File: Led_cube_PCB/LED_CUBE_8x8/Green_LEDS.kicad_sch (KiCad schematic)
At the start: 34 parts, among them IC1 74AHCT244PW,118, IC10 74AHCT244PW,118, IC11 74AHCT244PW,118, IC12 74AHCT244PW,118, IC2 74AHCT244PW,118, IC26 74AHC138PW,118, IC3 74AHCT244PW,118, IC8 74AHCT244PW,118, IC9 74AHCT244PW,118

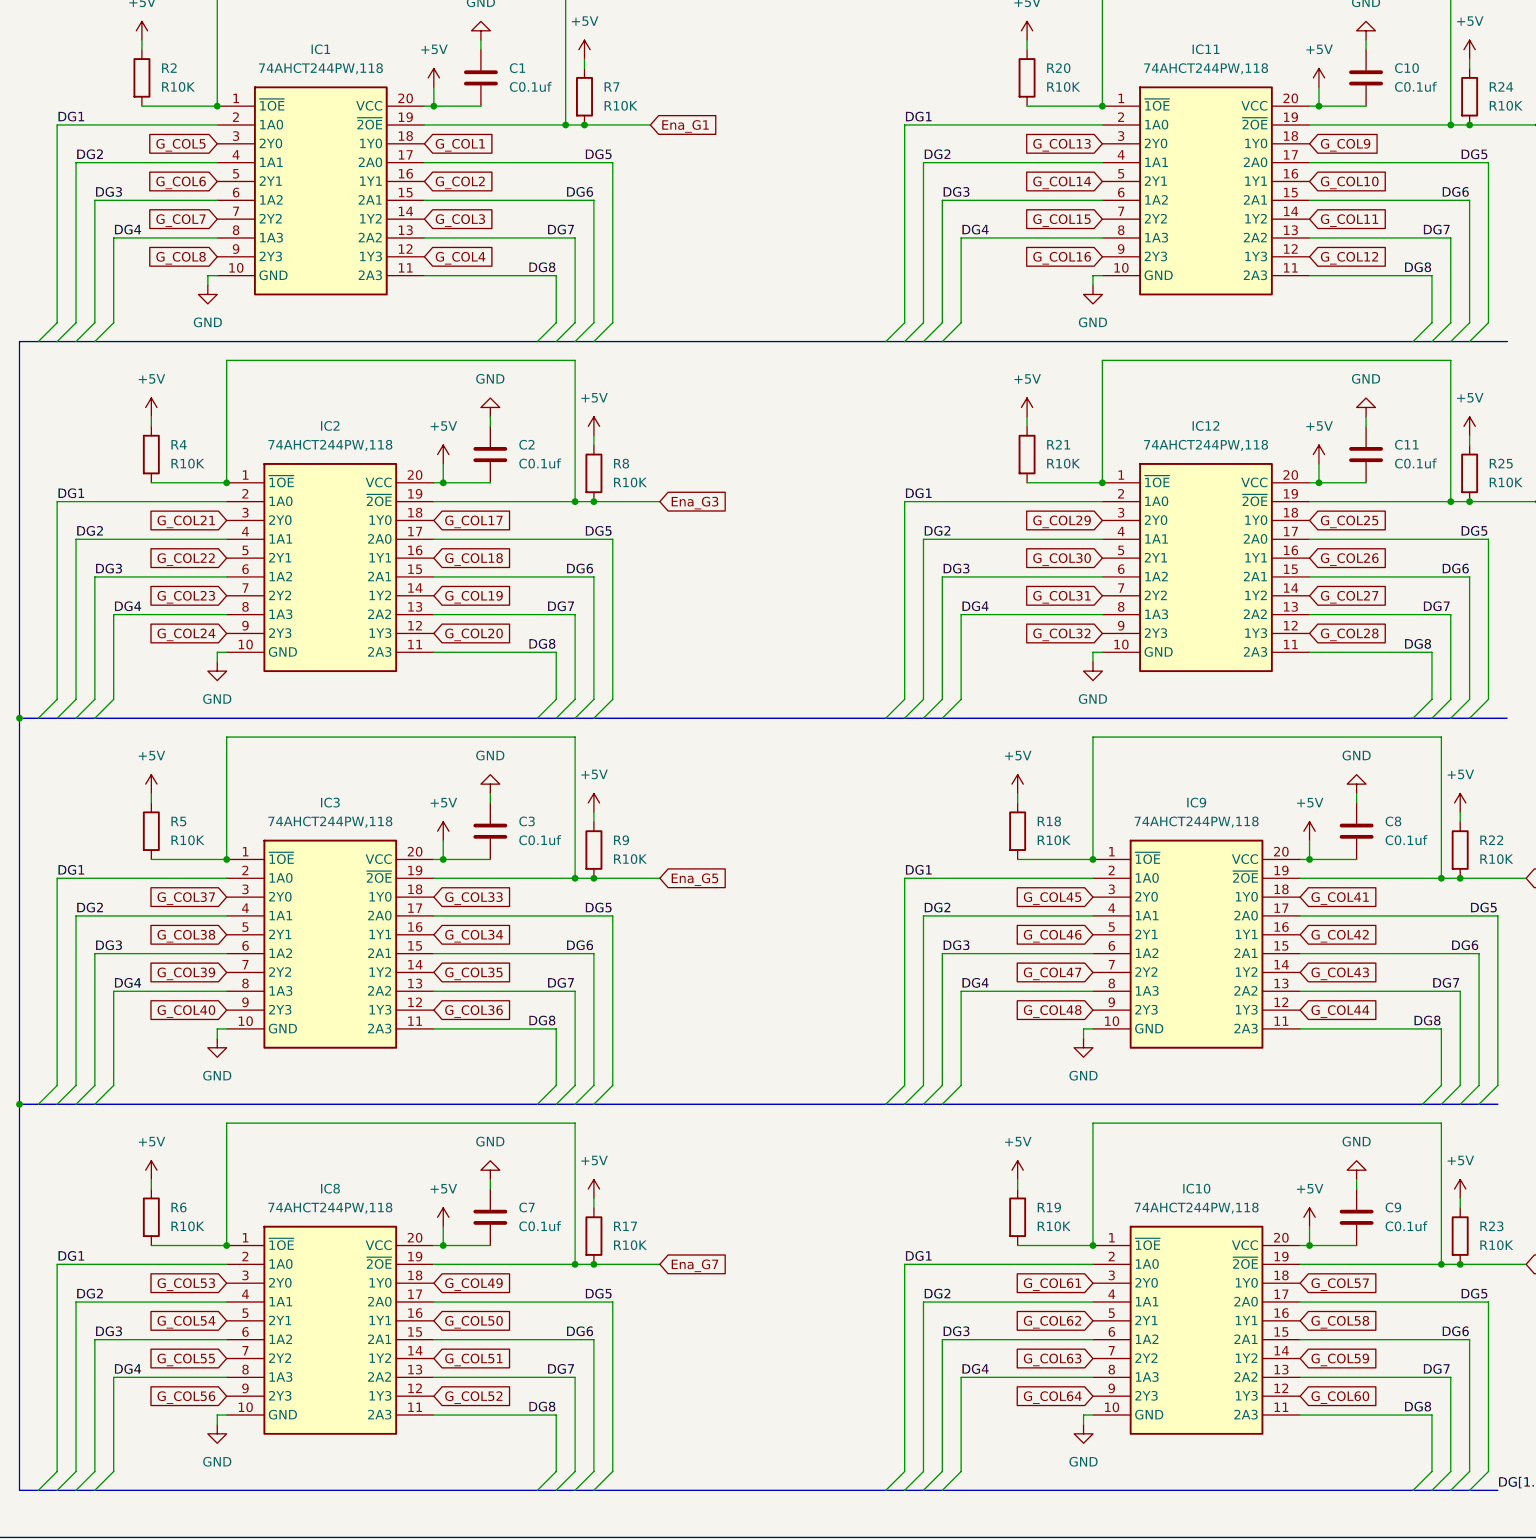
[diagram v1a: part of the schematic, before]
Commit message: added power schematic and updated labels to correct type e.g. output, input
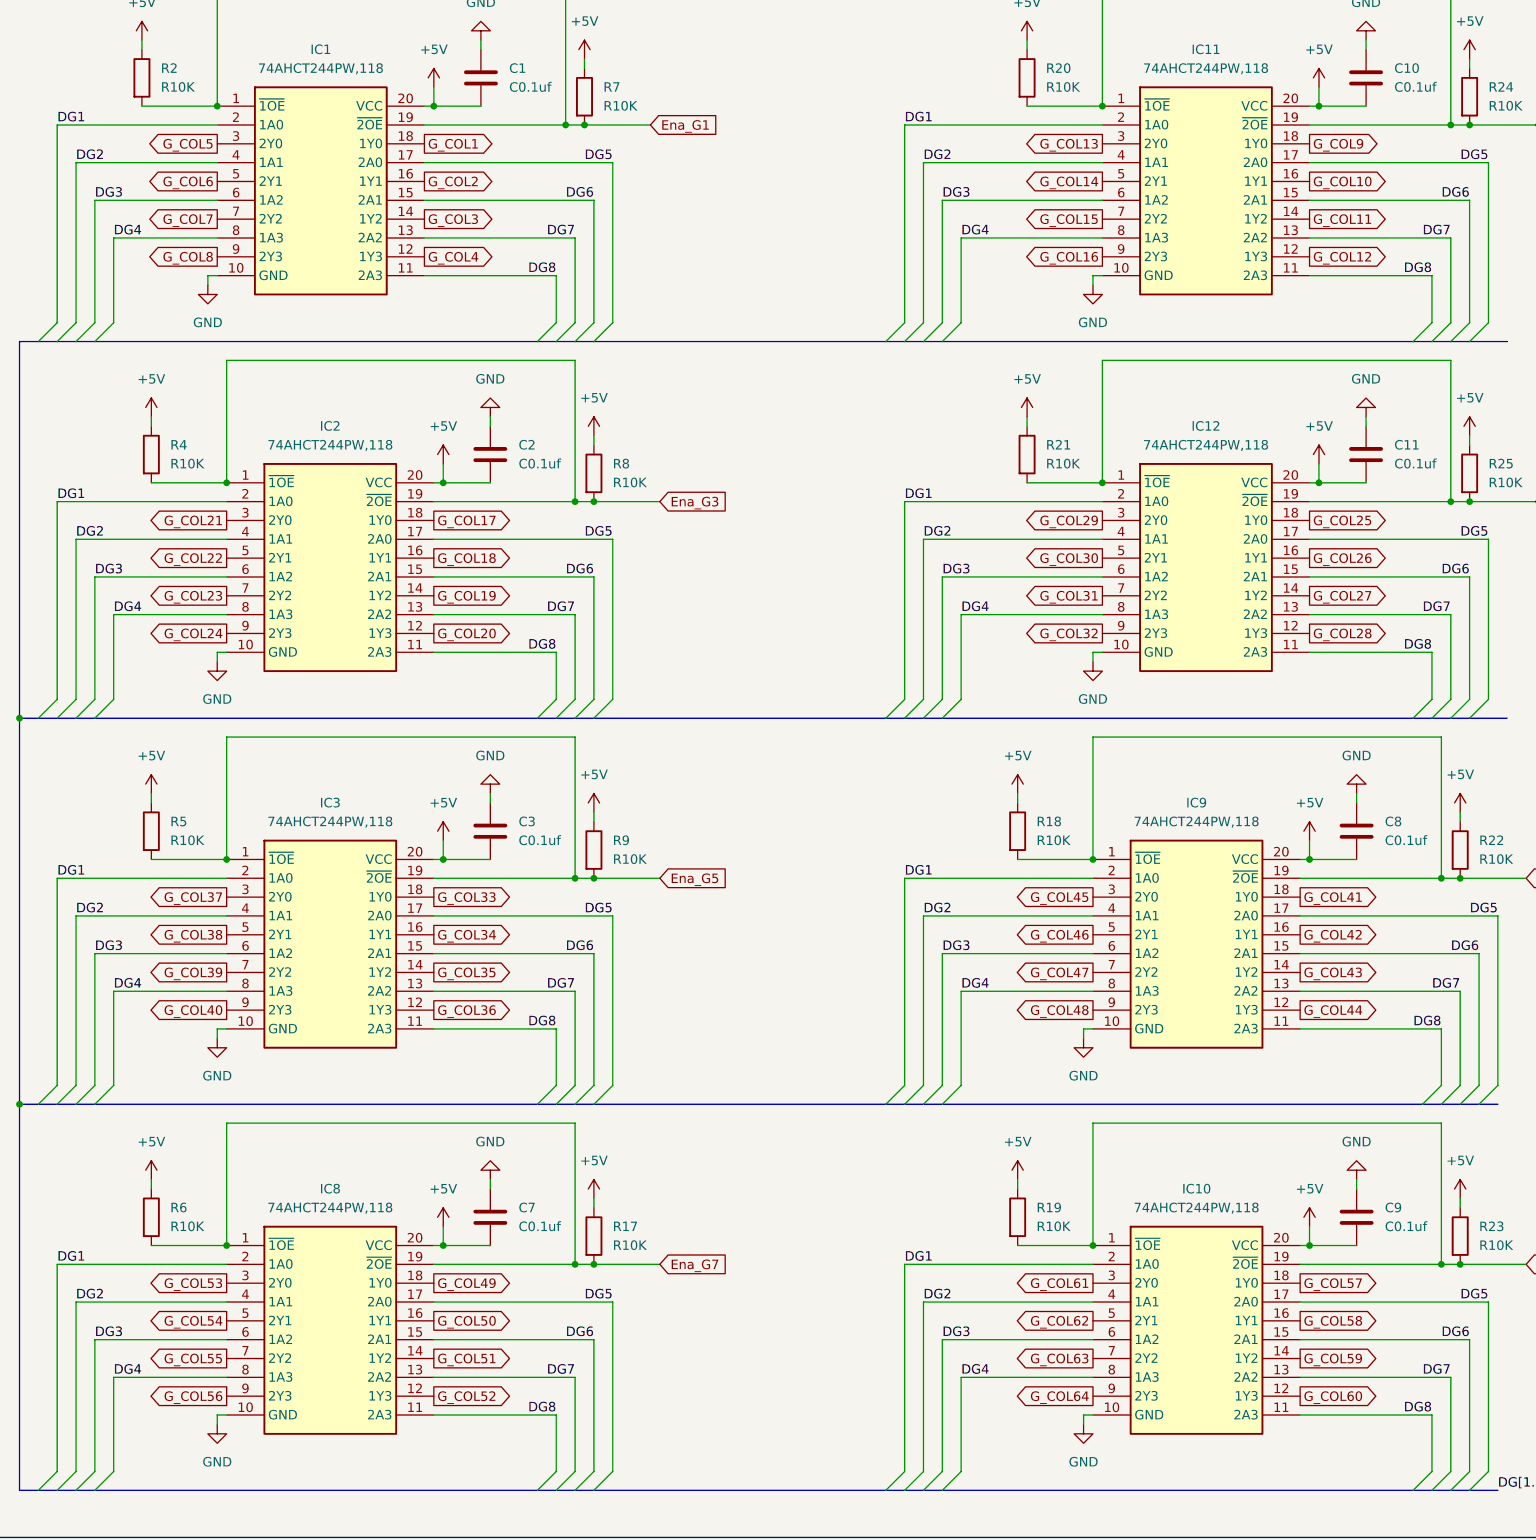
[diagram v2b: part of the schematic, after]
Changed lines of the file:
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@@
 	)
 	(global_label "G_COL12"
-		(shape input)
+		(shape output)
 		(at 203.2 58.42 0)
 		(fields_autoplaced yes)
@@
 	)
 	(global_label "G_COL32"
-		(shape input)
+		(shape output)
 		(at 175.26 109.22 180)
 		(fields_autoplaced yes)
@@
 	)
 	(global_label "G_COL31"
-		(shape input)
+		(shape output)
 		(at 175.26 104.14 180)
 		(fields_autoplaced yes)
@@
 	)
 	(global_label "G_COL15"
-		(shape input)
+		(shape output)
 		(at 175.26 53.34 180)
 		(fields_autoplaced yes)
@@
 	)
 	(global_label "G_COL20"
-		(shape input)
+		(shape output)
 		(at 85.09 109.22 0)
 		(fields_autoplaced yes)
@@
 	)
 	(global_label "G_COL24"
-		(shape input)
+		(shape output)
 		(at 57.15 109.22 180)
 		(fields_autoplaced yes)
@@
 	)
 	(global_label "G_COL13"
-		(shape input)
+		(shape output)
 		(at 175.26 43.18 180)
 		(fields_autoplaced yes)
@@
 	)
 	(global_label "G_COL2"
-		(shape input)
+		(shape output)
 		(at 83.82 48.26 0)
 		(fields_autoplaced yes)
@@
 	)
 	(global_label "G_COL35"
-		(shape input)
+		(shape output)
 		(at 85.09 154.94 0)
 		(fields_autoplaced yes)
@@
 	)
 	(global_label "G_COL49"
-		(shape input)
+		(shape output)
 		(at 85.09 196.85 0)
 		(fields_autoplaced yes)
@@
 	)
 	(global_label "G_COL6"
-		(shape input)
+		(shape output)
 		(at 55.88 48.26 180)
 		(fields_autoplaced yes)
@@
 	)
 	(global_label "G_COL62"
-		(shape input)
+		(shape output)
 		(at 173.99 201.93 180)
 		(fields_autoplaced yes)
@@
 	)
 	(global_label "G_COL7"
-		(shape input)
+		(shape output)
 		(at 55.88 53.34 180)
 		(fields_autoplaced yes)
@@
 	)
 	(global_label "G_COL14"
-		(shape input)
+		(shape output)
 		(at 175.26 48.26 180)
 		(fields_autoplaced yes)
@@
 	)
 	(global_label "G_COL36"
-		(shape input)
+		(shape output)
 		(at 85.09 160.02 0)
 		(fields_autoplaced yes)
@@
 	)
 	(global_label "G_COL16"
-		(shape input)
+		(shape output)
 		(at 175.26 58.42 180)
 		(fields_autoplaced yes)
@@
 	)
 	(global_label "G_COL48"
-		(shape input)
+		(shape output)
 		(at 173.99 160.02 180)
 		(fields_autoplaced yes)
@@
 	)
 	(global_label "G_COL25"
-		(shape input)
+		(shape output)
 		(at 203.2 93.98 0)
 		(fields_autoplaced yes)
@@
 	)
 	(global_label "G_COL33"
-		(shape input)
+		(shape output)
 		(at 85.09 144.78 0)
 		(fields_autoplaced yes)
@@
 	)
 	(global_label "G_COL58"
-		(shape input)
+		(shape output)
 		(at 201.93 201.93 0)
 		(fields_autoplaced yes)
@@
 	)
 	(global_label "G_COL57"
-		(shape input)
+		(shape output)
 		(at 201.93 196.85 0)
 		(fields_autoplaced yes)
@@
 	)
 	(global_label "G_COL50"
-		(shape input)
+		(shape output)
 		(at 85.09 201.93 0)
 		(fields_autoplaced yes)
@@
 	)
 	(global_label "G_COL61"
-		(shape input)
+		(shape output)
 		(at 173.99 196.85 180)
 		(fields_autoplaced yes)
@@
 	)
 	(global_label "G_COL11"
-		(shape input)
+		(shape output)
 		(at 203.2 53.34 0)
 		(fields_autoplaced yes)
@@
 	)
 	(global_label "G_COL3"
-		(shape input)
+		(shape output)
 		(at 83.82 53.34 0)
 		(fields_autoplaced yes)
@@
 	)
 	(global_label "G_COL39"
-		(shape input)
+		(shape output)
 		(at 57.15 154.94 180)
 		(fields_autoplaced yes)
@@
 	)
 	(global_label "G_COL1"
-		(shape input)
+		(shape output)
 		(at 83.82 43.18 0)
 		(fields_autoplaced yes)
@@
 	)
 	(global_label "G_COL64"
-		(shape input)
+		(shape output)
 		(at 173.99 212.09 180)
 		(fields_autoplaced yes)
@@
 	)
 	(global_label "G_COL23"
-		(shape input)
+		(shape output)
 		(at 57.15 104.14 180)
 		(fields_autoplaced yes)
@@
 	)
 	(global_label "G_COL55"
-		(shape input)
+		(shape output)
 		(at 57.15 207.01 180)
 		(fields_autoplaced yes)
@@
 	)
 	(global_label "G_COL22"
-		(shape input)
+		(shape output)
 		(at 57.15 99.06 180)
 		(fields_autoplaced yes)
@@
 	)
 	(global_label "G_COL43"
-		(shape input)
+		(shape output)
 		(at 201.93 154.94 0)
 		(fields_autoplaced yes)
@@
 	)
 	(global_label "G_COL60"
-		(shape input)
+		(shape output)
 		(at 201.93 212.09 0)
 		(fields_autoplaced yes)
@@
 	)
 	(global_label "G_COL28"
-		(shape input)
+		(shape output)
 		(at 203.2 109.22 0)
 		(fields_autoplaced yes)
@@
 	)
 	(global_label "G_COL17"
-		(shape input)
+		(shape output)
 		(at 85.09 93.98 0)
 		(fields_autoplaced yes)
@@
 	)
 	(global_label "G_COL42"
-		(shape input)
+		(shape output)
 		(at 201.93 149.86 0)
 		(fields_autoplaced yes)
@@
 	)
 	(global_label "G_COL8"
-		(shape input)
+		(shape output)
 		(at 55.88 58.42 180)
 		(fields_autoplaced yes)
@@
 	)
 	(global_label "G_COL30"
-		(shape input)
+		(shape output)
 		(at 175.26 99.06 180)
 		(fields_autoplaced yes)
@@
 	)
 	(global_label "G_COL40"
-		(shape input)
+		(shape output)
 		(at 57.15 160.02 180)
 		(fields_autoplaced yes)
@@
 	)
 	(global_label "G_COL21"
-		(shape input)
+		(shape output)
 		(at 57.15 93.98 180)
 		(fields_autoplaced yes)
@@
 	)
 	(global_label "G_COL53"
-		(shape input)
+		(shape output)
 		(at 57.15 196.85 180)
 		(fields_autoplaced yes)
@@
 	)
 	(global_label "G_COL34"
-		(shape input)
+		(shape output)
 		(at 85.09 149.86 0)
 		(fields_autoplaced yes)
@@
 	)
 	(global_label "G_COL27"
-		(shape input)
+		(shape output)
 		(at 203.2 104.14 0)
 		(fields_autoplaced yes)
@@
 	)
 	(global_label "G_COL54"
-		(shape input)
+		(shape output)
 		(at 57.15 201.93 180)
 		(fields_autoplaced yes)
@@
 	)
 	(global_label "G_COL19"
-		(shape input)
+		(shape output)
 		(at 85.09 104.14 0)
 		(fields_autoplaced yes)
@@
 	)
 	(global_label "G_COL4"
-		(shape input)
+		(shape output)
 		(at 83.82 58.42 0)
 		(fields_autoplaced yes)
@@
 	)
 	(global_label "G_COL44"
-		(shape input)
+		(shape output)
 		(at 201.93 160.02 0)
 		(fields_autoplaced yes)
@@
 	)
 	(global_label "G_COL46"
-		(shape input)
+		(shape output)
 		(at 173.99 149.86 180)
 		(fields_autoplaced yes)
@@
 	)
 	(global_label "G_COL47"
-		(shape input)
+		(shape output)
 		(at 173.99 154.94 180)
 		(fields_autoplaced yes)
@@
 	)
 	(global_label "G_COL5"
-		(shape input)
+		(shape output)
 		(at 55.88 43.18 180)
 		(fields_autoplaced yes)
@@
 	)
 	(global_label "G_COL63"
-		(shape input)
+		(shape output)
 		(at 173.99 207.01 180)
 		(fields_autoplaced yes)
@@
 	)
 	(global_label "G_COL59"
-		(shape input)
+		(shape output)
 		(at 201.93 207.01 0)
 		(fields_autoplaced yes)
@@
 	)
 	(global_label "G_COL52"
-		(shape input)
+		(shape output)
 		(at 85.09 212.09 0)
 		(fields_autoplaced yes)
@@
 	)
 	(global_label "G_COL37"
-		(shape input)
+		(shape output)
 		(at 57.15 144.78 180)
 		(fields_autoplaced yes)
@@
 	)
 	(global_label "G_COL51"
-		(shape input)
+		(shape output)
 		(at 85.09 207.01 0)
 		(fields_autoplaced yes)
@@
 	)
 	(global_label "G_COL9"
-		(shape input)
+		(shape output)
 		(at 203.2 43.18 0)
 		(fields_autoplaced yes)
@@
 	)
 	(global_label "G_COL56"
-		(shape input)
+		(shape output)
 		(at 57.15 212.09 180)
 		(fields_autoplaced yes)
@@
 	)
 	(global_label "G_COL10"
-		(shape input)
+		(shape output)
 		(at 203.2 48.26 0)
 		(fields_autoplaced yes)
@@
 	)
 	(global_label "G_COL26"
-		(shape input)
+		(shape output)
 		(at 203.2 99.06 0)
 		(fields_autoplaced yes)
@@
 	)
 	(global_label "G_COL38"
-		(shape input)
+		(shape output)
 		(at 57.15 149.86 180)
 		(fields_autoplaced yes)
@@
 	)
 	(global_label "G_COL18"
-		(shape input)
+		(shape output)
 		(at 85.09 99.06 0)
 		(fields_autoplaced yes)
@@
 	)
 	(global_label "G_COL45"
-		(shape input)
+		(shape output)
 		(at 173.99 144.78 180)
 		(fields_autoplaced yes)
@@
 	)
 	(global_label "G_COL41"
-		(shape input)
+		(shape output)
 		(at 201.93 144.78 0)
 		(fields_autoplaced yes)
@@
 	)
 	(global_label "G_COL29"
-		(shape input)
+		(shape output)
 		(at 175.26 93.98 180)
 		(fields_autoplaced yes)

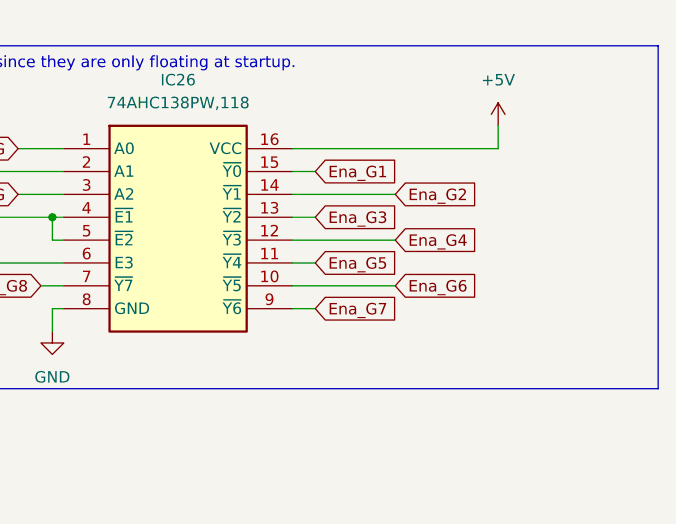
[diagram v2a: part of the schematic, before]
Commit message: added 3.3V power supply for microcontroller and started on STM schematic.
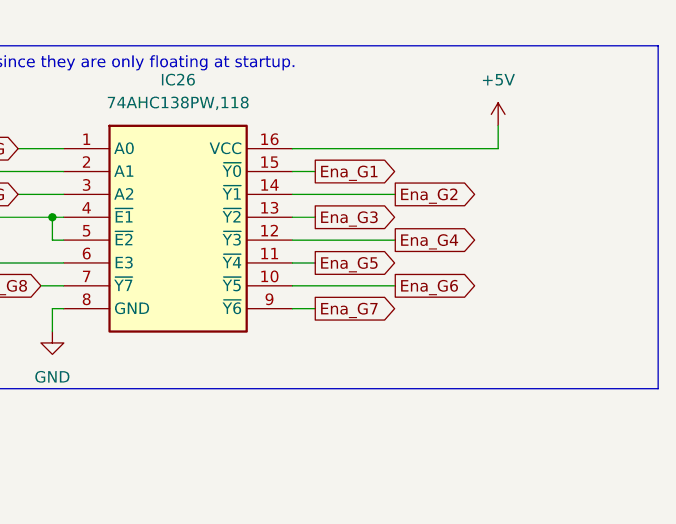
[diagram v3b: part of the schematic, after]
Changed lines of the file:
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@@
 	)
 	(global_label "Ena_G5"
-		(shape input)
+		(shape output)
 		(at 365.76 40.64 0)
 		(fields_autoplaced yes)
@@
 	)
 	(global_label "Ena_G6"
-		(shape input)
+		(shape output)
 		(at 374.65 43.18 0)
 		(fields_autoplaced yes)
@@
 	)
 	(global_label "Ena_G2"
-		(shape input)
+		(shape output)
 		(at 374.65 33.02 0)
 		(fields_autoplaced yes)
@@
 	)
 	(global_label "Ena_G7"
-		(shape input)
+		(shape output)
 		(at 365.76 45.72 0)
 		(fields_autoplaced yes)
@@
 	)
 	(global_label "Ena_G4"
-		(shape input)
+		(shape output)
 		(at 374.65 38.1 0)
 		(fields_autoplaced yes)
@@
 	)
 	(global_label "Ena_G1"
-		(shape input)
+		(shape output)
 		(at 365.76 30.48 0)
 		(fields_autoplaced yes)
@@
 	)
 	(global_label "Ena_G3"
-		(shape input)
+		(shape output)
 		(at 365.76 35.56 0)
 		(fields_autoplaced yes)
